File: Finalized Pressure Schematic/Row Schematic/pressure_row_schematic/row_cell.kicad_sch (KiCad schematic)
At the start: 0 parts

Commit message: Worked on V1
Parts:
- added TP, TP10, TP11, TP12, TP13, TP14, TP15, TP16, TP17, TP18, TP19, TP2, TP20, TP21, TP22, TP23, TP24, TP25, TP26, TP3, TP4, TP5, TP6, TP7, TP8, TP9: TestPoint, symbol Connector:TestPoint
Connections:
- new net ROW_OUT: TP.1, TP10.1, TP11.1, TP12.1, TP13.1, TP14.1, TP15.1, TP16.1, TP17.1, TP18.1, TP19.1, TP2.1, TP20.1, TP21.1, TP22.1, TP23.1, TP24.1, TP25.1, TP26.1, TP3.1, TP4.1, TP5.1, TP6.1, TP7.1, TP8.1, TP9.1
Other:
- note added: "LionStride"

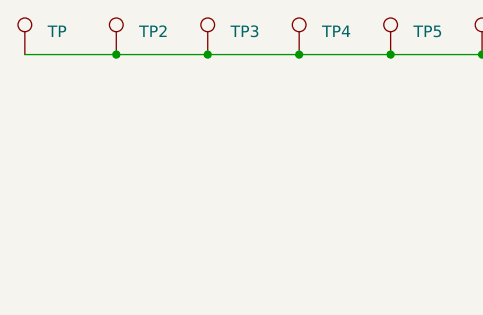
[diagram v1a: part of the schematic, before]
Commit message: Added missing revision date and title
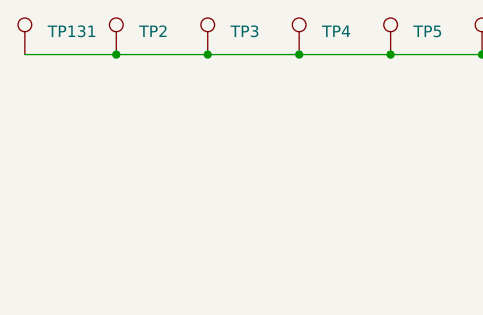
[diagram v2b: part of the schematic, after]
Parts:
- renumbered TP to TP131
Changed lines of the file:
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@@
 		(on_board yes)
 		(dnp no)
-		(property "Reference" "TP"
+		(property "Reference" "TP?"
 			(at 24.13 34.29 0)
 			(effects
@@
 					(unit 1)
 				)
+				(path "/e39b7473-fb25-4371-8fdc-05ae0c233266/32a90ac2-0c66-426c-b2ef-ef7dc129a741"
+					(reference "TP?")
+					(unit 1)
+				)
